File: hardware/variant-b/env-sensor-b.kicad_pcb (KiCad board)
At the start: 4 copper layers, 30 x 51 mm, 64 parts, among them J1 USB-C 16P, J2 Molex PicoBlade 3P, Q1 2N7002, SW1 SW_PROV, U1 ESP32-C6-MINI-1-N4, U2 SHT45-AD1F, U3 TPS62840DLC, U4 BQ24074RGTR, U5 USBLC6-2SC6

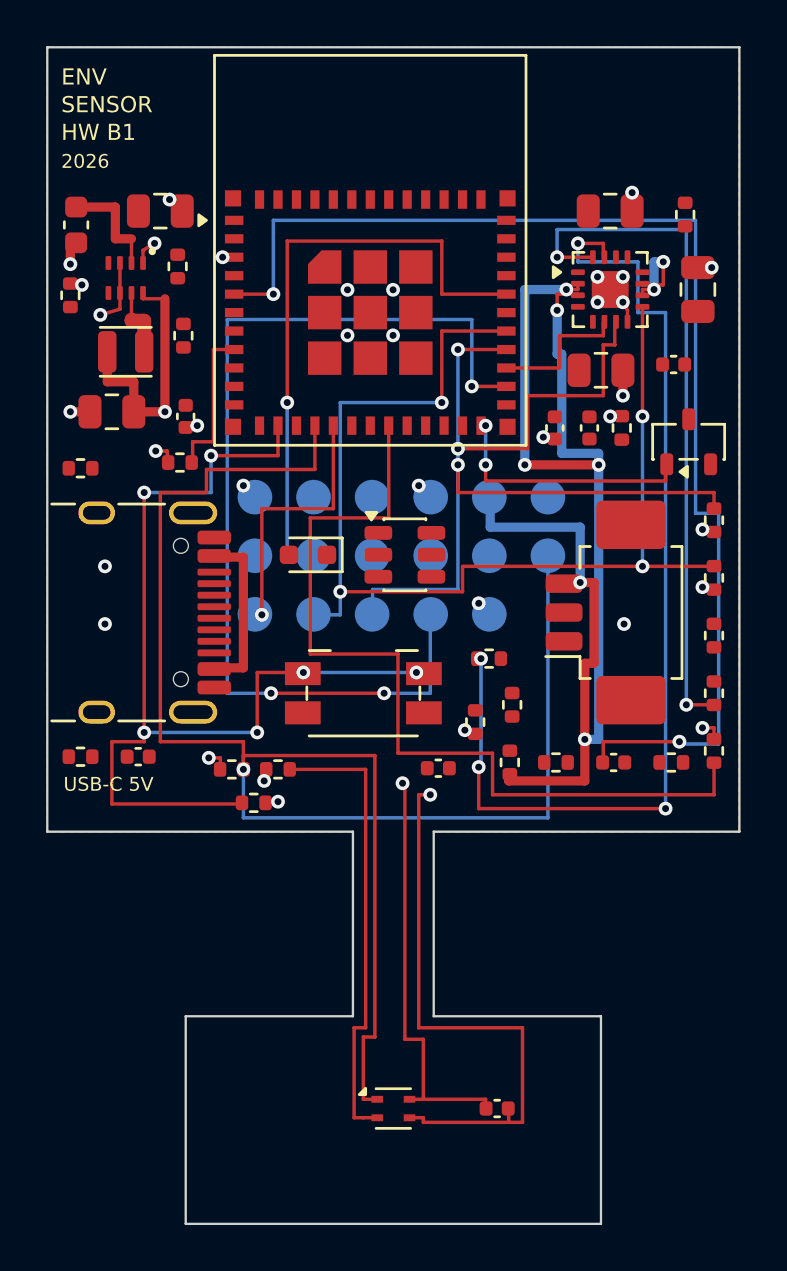
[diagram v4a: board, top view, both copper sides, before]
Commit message: build(boardgen): regenerate local charger power routes
Regenerate both boards and model SVGs from the preceding charger-bypass source change. A47/B45 unconnected items remain explicitly recorded.
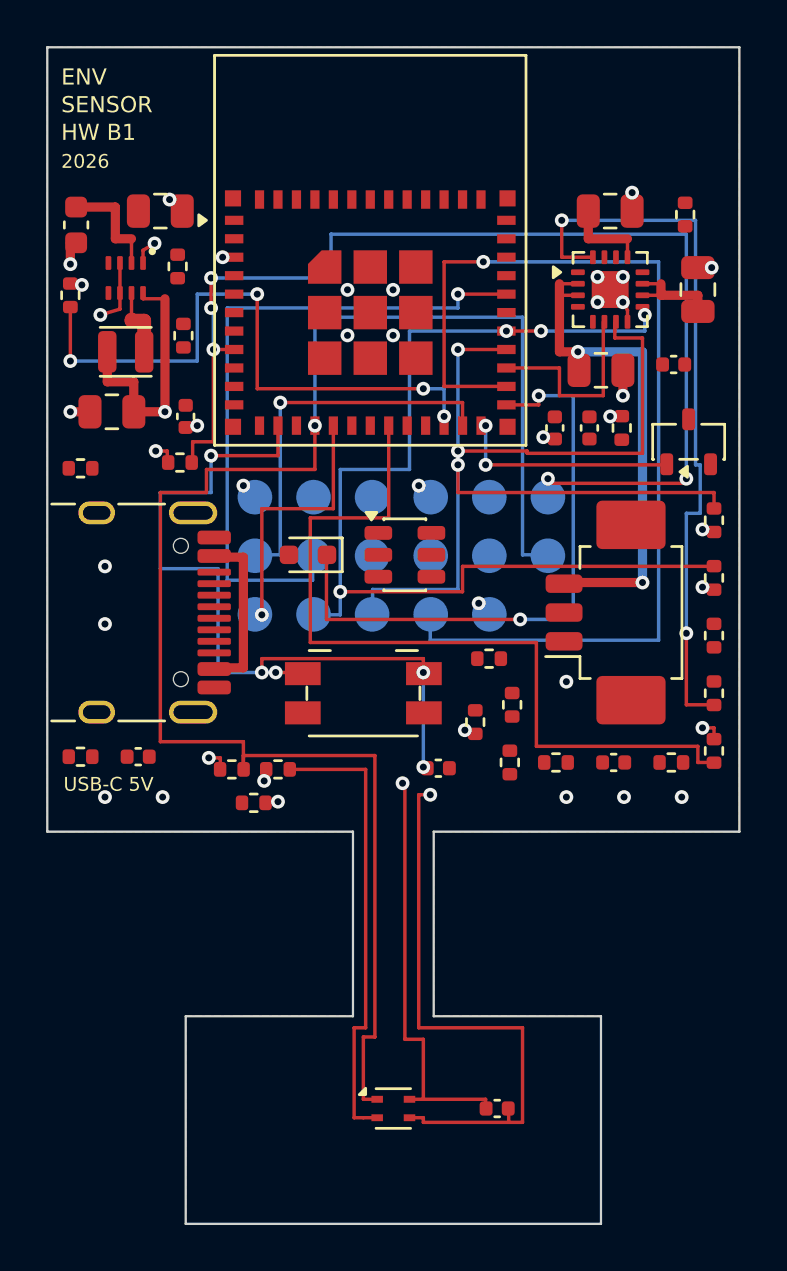
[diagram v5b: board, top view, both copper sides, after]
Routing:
- net VBAT_SENSE: track 52.9 -> 0.00 mm, vias 2 -> 0
- net ITERM: track 44.7 -> 0.00 mm, vias 4 -> 0
- net EN: track 6.70 -> 50.2 mm, vias 0 -> 5
- net VBAT: track 57.6 -> 23.2 mm, vias 6 -> 2
- net BOOT_MODE_H: track 0.00 -> 27.1 mm, vias 0 -> 4
- net LED_N: track 0.00 -> 26.5 mm, vias 0 -> 2
- net BOOT_N: track 0.00 -> 16.6 mm, vias 0 -> 1
- net BTN_PROV: track 43.9 -> 34.3 mm, vias 6 -> 5
- net CHG_N: track 49.3 -> 45.2 mm
- net VBUS: track 7.60 -> 11.3 mm
- net USB_EN2: track 38.3 -> 35.5 mm
- net UART_TX: track 26.5 -> 29.3 mm
- net PG_N: track 42.6 -> 45.3 mm
- net USB_ISEL: track 6.20 -> 8.60 mm
- net ISET: track 30.1 -> 31.7 mm
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
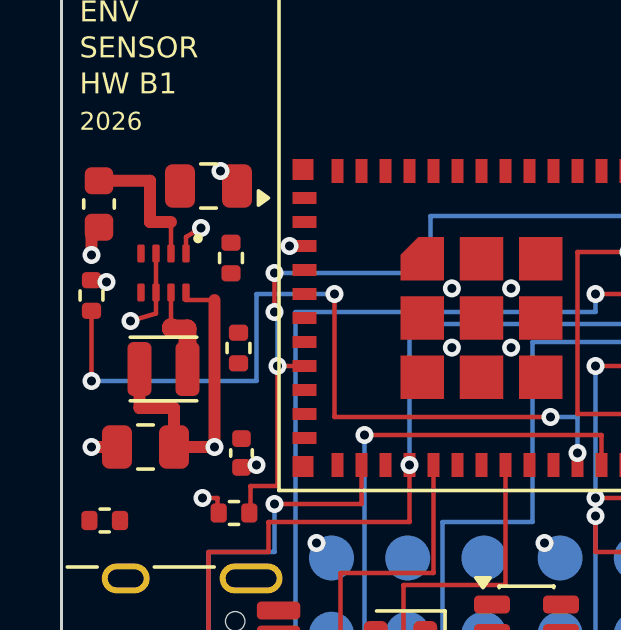
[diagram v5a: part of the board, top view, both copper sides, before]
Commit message: build(boardgen): regenerate regulator control routing
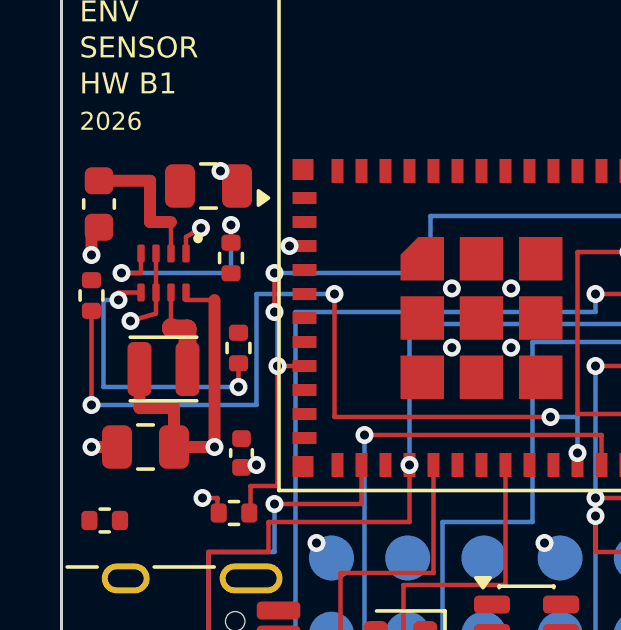
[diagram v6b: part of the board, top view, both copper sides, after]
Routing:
- net VSET: track 0.00 -> 9.69 mm, vias 0 -> 2
- net EN_REG: track 0.00 -> 7.14 mm, vias 0 -> 2
- net BOOT_MODE_H: track 27.1 -> 28.7 mm
- net +3V0: track 47.0 -> 46.4 mm, vias 17 -> 16
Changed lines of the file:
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@@
 	)
 	(segment
+		(start 102.65 69.35)
+		(end 102.65 70.0)
+		(width 0.15)
+		(layer "F.Cu")
+		(net 11)
+	)
+	(segment
+		(start 102.65 70.0)
+		(end 102.0 70.0)
+		(width 0.15)
+		(layer "F.Cu")
+		(net 11)
+	)
+	(segment
+		(start 105.65 68.99)
+		(end 105.65 68.4)
+		(width 0.15)
+		(layer "F.Cu")
+		(net 11)
+	)
+	(segment
+		(start 102.0 70.0)
+		(end 105.65 70.0)
+		(width 0.15)
+		(layer "B.Cu")
+		(net 11)
+	)
+	(segment
+		(start 105.65 70.0)
+		(end 105.65 68.4)
+		(width 0.15)
+		(layer "B.Cu")
+		(net 11)
+	)
+	(segment
+		(start 102.65 70.65)
+		(end 101.9 70.65)
+		(width 0.15)
+		(layer "F.Cu")
+		(net 34)
+	)
+	(segment
+		(start 101.9 70.65)
+		(end 101.9 70.9)
+		(width 0.15)
+		(layer "F.Cu")
+		(net 34)
+	)
+	(segment
+		(start 105.9 73.01)
+		(end 105.9 73.8)
+		(width 0.15)
+		(layer "F.Cu")
+		(net 34)
+	)
+	(segment
+		(start 101.9 70.9)
+		(end 101.4 70.9)
+		(width 0.15)
+		(layer "B.Cu")
+		(net 34)
+	)
+	(segment
+		(start 101.4 70.9)
+		(end 101.4 73.8)
+		(width 0.15)
+		(layer "B.Cu")
+		(net 34)
+	)
+	(segment
+		(start 101.4 73.8)
+		(end 105.9 73.8)
+		(width 0.15)
+		(layer "B.Cu")
+		(net 34)
+	)
+	(segment
 		(start 109.0 79.5)
 		(end 109.0 79.0)
@@
 	)
 	(segment
-		(start 101.0 70.2)
-		(end 101.0 70.3)
-		(width 0.15)
-		(layer "F.Cu")
-		(net 1)
-	)
-	(segment
-		(start 101.0 70.3)
-		(end 101.5 70.3)
-		(width 0.15)
-		(layer "F.Cu")
-		(net 1)
-	)
-	(segment
 		(start 107.2 82.0)
 		(end 107.2 82.1)
@@
 	(segment
 		(start 106.5 70.7)
-		(end 106.5 73.6)
+		(end 106.5 74.4)
 		(width 0.15)
 		(layer "B.Cu")
@@
 	)
 	(segment
-		(start 106.5 73.6)
-		(end 101.0 73.6)
+		(start 106.5 74.4)
+		(end 101.0 74.4)
 		(width 0.15)
 		(layer "B.Cu")
@@
 	)
 	(segment
-		(start 101.0 73.6)
+		(start 101.0 74.4)
 		(end 101.0 71.3)
 		(width 0.15)
@@
 	)
 	(via
+		(at 102.0 70.0)
+		(size 0.6)
+		(drill 0.3)
+		(layers "F.Cu" "B.Cu")
+		(net 11)
+	)
+	(via
+		(at 105.65 68.4)
+		(size 0.6)
+		(drill 0.3)
+		(layers "F.Cu" "B.Cu")
+		(net 11)
+	)
+	(via
+		(at 101.9 70.9)
+		(size 0.6)
+		(drill 0.3)
+		(layers "F.Cu" "B.Cu")
+		(net 34)
+	)
+	(via
+		(at 105.9 73.8)
+		(size 0.6)
+		(drill 0.3)
+		(layers "F.Cu" "B.Cu")
+		(net 34)
+	)
+	(via
 		(at 108.5 79.0)
 		(size 0.6)
@@
 	)
 	(via
-		(at 101.5 70.3)
-		(size 0.6)
-		(drill 0.3)
-		(layers "F.Cu" "B.Cu")
-		(net 1)
-	)
-	(via
 		(at 117.8 73.1)
 		(size 0.6)
@@
 	)
 	(via
-		(at 101.0 73.6)
+		(at 101.0 74.4)
 		(size 0.6)
 		(drill 0.3)
@@
 		(net_name "")
 		(layers "B.Cu")
-		(name "Power escape GND 34 0")
+		(name "Power escape GND 40 0")
 		(hatch edge 0.5)
 		(connect_pads
@@
 		(net_name "")
 		(layers "B.Cu")
-		(name "Power escape GND 34 1")
+		(name "Power escape GND 40 1")
 		(hatch edge 0.5)
 		(connect_pads
@@
 		(net_name "")
 		(layers "B.Cu")
-		(name "Power escape GND 35 0")
+		(name "Power escape GND 41 0")
 		(hatch edge 0.5)
 		(connect_pads
@@
 		(net_name "")
 		(layers "B.Cu")
-		(name "Power escape GND 35 1")
+		(name "Power escape GND 41 1")
 		(hatch edge 0.5)
 		(connect_pads
@@
 		(net_name "")
 		(layers "F.Cu")
-		(name "Power escape +3V0 36 0")
+		(name "Power escape +3V0 42 0")
 		(hatch edge 0.5)
 		(connect_pads
@@
 		(net_name "")
 		(layers "F.Cu")
-		(name "Power escape +3V0 37 0")
+		(name "Power escape +3V0 43 0")
 		(hatch edge 0.5)
 		(connect_pads
@@
 		(net_name "")
 		(layers "F.Cu")
-		(name "Power escape +3V0 37 1")
+		(name "Power escape +3V0 43 1")
 		(hatch edge 0.5)
 		(connect_pads
@@
 		(net_name "")
 		(layers "F.Cu")
-		(name "Power escape +3V0 38 0")
+		(name "Power escape +3V0 44 0")
 		(hatch edge 0.5)
 		(connect_pads
@@
 		(net_name "")
 		(layers "F.Cu")
-		(name "Power escape +3V0 38 1")
+		(name "Power escape +3V0 44 1")
 		(hatch edge 0.5)
 		(connect_pads
@@
 		(net_name "")
 		(layers "B.Cu")
-		(name "Power escape +3V0 39 0")
+		(name "Power escape +3V0 45 0")
 		(hatch edge 0.5)
 		(connect_pads
@@
 		(net_name "")
 		(layers "B.Cu")
-		(name "Power escape +3V0 39 1")
+		(name "Power escape +3V0 45 1")
 		(hatch edge 0.5)
 		(connect_pads
@@
 		(net_name "")
 		(layers "F.Cu")
-		(name "Power escape +3V0 40 0")
+		(name "Power escape +3V0 46 0")
 		(hatch edge 0.5)
 		(connect_pads
@@
 		(net_name "")
 		(layers "F.Cu")
-		(name "Power escape +3V0 40 1")
+		(name "Power escape +3V0 46 1")
 		(hatch edge 0.5)
 		(connect_pads
@@
 		(net_name "")
 		(layers "F.Cu")
-		(name "Power escape +3V0 41 0")
+		(name "Power escape +3V0 47 0")
 		(hatch edge 0.5)
 		(connect_pads
@@
 		(net_name "")
 		(layers "F.Cu")
-		(name "Power escape +3V0 41 1")
+		(name "Power escape +3V0 47 1")
 		(hatch edge 0.5)
 		(connect_pads
@@
 		(net_name "")
 		(layers "F.Cu")
-		(name "Power escape +3V0 42 0")
+		(name "Power escape +3V0 48 0")
 		(hatch edge 0.5)
 		(connect_pads
@@
 		(net_name "")
 		(layers "F.Cu")
-		(name "Power escape +3V0 42 1")
+		(name "Power escape +3V0 48 1")
 		(hatch edge 0.5)
 		(connect_pads
@@
 		(net_name "")
 		(layers "F.Cu")
-		(name "Power escape +3V0 43 0")
+		(name "Power escape +3V0 49 0")
 		(hatch edge 0.5)
 		(connect_pads
@@
 		(net_name "")
 		(layers "F.Cu")
-		(name "Power escape +3V0 43 1")
+		(name "Power escape +3V0 49 1")
 		(hatch edge 0.5)
 		(connect_pads
@@
 		(net_name "")
 		(layers "F.Cu")
-		(name "Power escape +3V0 44 0")
+		(name "Power escape +3V0 50 0")
 		(hatch edge 0.5)
 		(connect_pads
@@
 		(net_name "")
 		(layers "F.Cu")
-		(name "Power escape +3V0 44 1")
+		(name "Power escape +3V0 50 1")
 		(hatch edge 0.5)
 		(connect_pads
@@
 		(net_name "")
 		(layers "F.Cu")
-		(name "Power escape +3V0 45 0")
+		(name "Power escape +3V0 51 0")
 		(hatch edge 0.5)
 		(connect_pads
@@
 		(net_name "")
 		(layers "F.Cu")
-		(name "Power escape +3V0 46 0")
+		(name "Power escape +3V0 52 0")
 		(hatch edge 0.5)
 		(connect_pads
@@
 		(net_name "")
 		(layers "F.Cu")
-		(name "Power escape +3V0 46 1")
+		(name "Power escape +3V0 52 1")
 		(hatch edge 0.5)
 		(connect_pads
@@
 		(net_name "")
 		(layers "F.Cu")
-		(name "Power escape +3V0 47 0")
+		(name "Power escape +3V0 53 0")
 		(hatch edge 0.5)
 		(connect_pads
@@
 		(net_name "")
 		(layers "F.Cu")
-		(name "Power escape +3V0 47 1")
+		(name "Power escape +3V0 53 1")
 		(hatch edge 0.5)
 		(connect_pads
@@
 		(net_name "")
 		(layers "F.Cu")
-		(name "Power escape +3V0 48 0")
+		(name "Power escape +3V0 54 0")
 		(hatch edge 0.5)
 		(connect_pads
@@
 		(net_name "")
 		(layers "F.Cu")
-		(name "Power escape +3V0 48 1")
+		(name "Power escape +3V0 54 1")
 		(hatch edge 0.5)
 		(connect_pads
@@
 		(net_name "")
 		(layers "F.Cu")
-		(name "Power escape +3V0 49 0")
+		(name "Power escape +3V0 55 0")
 		(hatch edge 0.5)
 		(connect_pads
@@
 		(net_name "")
 		(layers "F.Cu")
-		(name "Power escape +3V0 49 1")
+		(name "Power escape +3V0 55 1")
 		(hatch edge 0.5)
 		(connect_pads
@@
 			)
 		)
-	)
-	(zone
-		(net 0)
-		(net_name "")
-		(layers "F.Cu")
-		(name "Power escape +3V0 50 0")
-		(hatch edge 0.5)
-		(connect_pads
-			(clearance 0.2)
-		)
-		(min_thickness 0.2)
-		(filled_areas_thickness no)
-		(keepout
-			(tracks allowed)
-			(vias allowed)
-			(pads allowed)
-			(copperpour allowed)
-			(footprints allowed)
-		)
-		(placement
-			(enabled no)
-			(sheetname "")
-		)
-		(fill
-			(thermal_gap 0.3)
-			(thermal_bridge_width 0.4)
-		)
-		(polygon
-			(pts
-				(xy 100.9 70.1) (xy 101.1 70.1) (xy 101.1 70.4) (xy 100.9 70.4)
-			)
-		)
-	)
-	(zone
-		(net 0)
-		(net_name "")
-		(layers "F.Cu")
-		(name "Power escape +3V0 50 1")
-		(hatch edge 0.5)
-		(connect_pads
-			(clearance 0.2)
-		)
-		(min_thickness 0.2)
-		(filled_areas_thickness no)
-		(keepout
-			(tracks allowed)
-			(vias allowed)
-			(pads allowed)
-			(copperpour allowed)
-			(footprints allowed)
-		)
-		(placement
-			(enabled no)
-			(sheetname "")
-		)
-		(fill
-			(thermal_gap 0.3)
-			(thermal_bridge_width 0.4)
-		)
-		(polygon
-			(pts
-				(xy 100.9 70.2) (xy 101.6 70.2) (xy 101.6 70.4) (xy 100.9 70.4)
-			)
-		)

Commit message: build(sch): regenerate connector mounting-ground connectivity
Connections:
- J2 pad MP: unconnected-(J2-MountPin-PadMP) -> GND
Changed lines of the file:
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@@
 	(net 36 "unconnected-(J1-SBU1-PadA8)")
 	(net 37 "unconnected-(J1-SBU2-PadB8)")
-	(net 38 "unconnected-(J2-MountPin-PadMP)")
-	(net 39 "unconnected-(U1-IO0-Pad12)")
-	(net 40 "unconnected-(U1-IO15-Pad20)")
-	(net 41 "unconnected-(U1-IO4-Pad9)")
-	(net 42 "unconnected-(U1-IO5-Pad10)")
-	(net 43 "unconnected-(U1-NC-Pad21)")
-	(net 44 "unconnected-(U1-NC-Pad32)")
-	(net 45 "unconnected-(U1-NC-Pad33)")
-	(net 46 "unconnected-(U1-NC-Pad34)")
-	(net 47 "unconnected-(U1-NC-Pad35)")
-	(net 48 "unconnected-(U1-NC-Pad4)")
-	(net 49 "unconnected-(U1-NC-Pad7)")
-	(net 50 "unconnected-(U4-TMR-Pad14)")
+	(net 38 "unconnected-(U1-IO0-Pad12)")
+	(net 39 "unconnected-(U1-IO15-Pad20)")
+	(net 40 "unconnected-(U1-IO4-Pad9)")
+	(net 41 "unconnected-(U1-IO5-Pad10)")
+	(net 42 "unconnected-(U1-NC-Pad21)")
+	(net 43 "unconnected-(U1-NC-Pad32)")
+	(net 44 "unconnected-(U1-NC-Pad33)")
+	(net 45 "unconnected-(U1-NC-Pad34)")
+	(net 46 "unconnected-(U1-NC-Pad35)")
+	(net 47 "unconnected-(U1-NC-Pad4)")
+	(net 48 "unconnected-(U1-NC-Pad7)")
+	(net 49 "unconnected-(U4-TMR-Pad14)")
 	(footprint "sensorly:ESP32-C6-MINI-1"
 		(layer "F.Cu")
@@
 			(size 0.8 0.4)
 			(layers "F.Cu" "F.Mask" "F.Paste")
-			(net 48 "unconnected-(U1-NC-Pad4)")
+			(net 47 "unconnected-(U1-NC-Pad4)")
 		)
 		(pad "5" smd rect
@@
 			(size 0.8 0.4)
 			(layers "F.Cu" "F.Mask" "F.Paste")
-			(net 49 "unconnected-(U1-NC-Pad7)")
+			(net 48 "unconnected-(U1-NC-Pad7)")
 		)
 		(pad "8" smd rect
@@
 			(size 0.8 0.4)
 			(layers "F.Cu" "F.Mask" "F.Paste")
-			(net 41 "unconnected-(U1-IO4-Pad9)")
+			(net 40 "unconnected-(U1-IO4-Pad9)")
 		)
 		(pad "10" smd rect
@@
 			(size 0.8 0.4)
 			(layers "F.Cu" "F.Mask" "F.Paste")
-			(net 42 "unconnected-(U1-IO5-Pad10)")
+			(net 41 "unconnected-(U1-IO5-Pad10)")
 		)
 		(pad "11" smd rect
@@
 			(size 0.8 0.4)
 			(layers "F.Cu" "F.Mask" "F.Paste")
-			(net 39 "unconnected-(U1-IO0-Pad12)")
+			(net 38 "unconnected-(U1-IO0-Pad12)")
 		)
 		(pad "13" smd rect
@@
 			(size 0.8 0.4)
 			(layers "F.Cu" "F.Mask" "F.Paste")
-			(net 40 "unconnected-(U1-IO15-Pad20)")
+			(net 39 "unconnected-(U1-IO15-Pad20)")
 		)
 		(pad "21" smd rect
@@
 			(size 0.8 0.4)
 			(layers "F.Cu" "F.Mask" "F.Paste")
-			(net 43 "unconnected-(U1-NC-Pad21)")
+			(net 42 "unconnected-(U1-NC-Pad21)")
 		)
 		(pad "22" smd rect
@@
 			(size 0.8 0.4)
 			(layers "F.Cu" "F.Mask" "F.Paste")
-			(net 44 "unconnected-(U1-NC-Pad32)")
+			(net 43 "unconnected-(U1-NC-Pad32)")
 		)
 		(pad "33" smd rect
@@
 			(size 0.8 0.4)
 			(layers "F.Cu" "F.Mask" "F.Paste")
-			(net 45 "unconnected-(U1-NC-Pad33)")
+			(net 44 "unconnected-(U1-NC-Pad33)")
 		)
 		(pad "34" smd rect
@@
 			(size 0.8 0.4)
 			(layers "F.Cu" "F.Mask" "F.Paste")
-			(net 46 "unconnected-(U1-NC-Pad34)")
+			(net 45 "unconnected-(U1-NC-Pad34)")
 		)
 		(pad "35" smd rect
@@
 			(size 0.8 0.4)
 			(layers "F.Cu" "F.Mask" "F.Paste")
-			(net 47 "unconnected-(U1-NC-Pad35)")
+			(net 46 "unconnected-(U1-NC-Pad35)")
 		)
 		(pad "36" smd rect
@@
 		(pad "MP" smd roundrect (at -3.8 0.5 90.0) (size 2.1 3)
 			(layers "F.Cu" "F.Mask" "F.Paste") (roundrect_rratio 0.119048)
-			(net 38 "unconnected-(J2-MountPin-PadMP)")
+			(net 12 "GND")
 		)
 		(pad "MP" smd roundrect (at 3.8 0.5 90.0) (size 2.1 3)
 			(layers "F.Cu" "F.Mask" "F.Paste") (roundrect_rratio 0.119048)
-			(net 38 "unconnected-(J2-MountPin-PadMP)")
+			(net 12 "GND")
 		)
 		(embedded_fonts no)
@@
 			(layers "F.Cu" "F.Mask" "F.Paste")
 			(roundrect_rratio 0.2)
-			(net 50 "unconnected-(U4-TMR-Pad14)")
+			(net 49 "unconnected-(U4-TMR-Pad14)")
 		)
 		(pad "15" smd roundrect
